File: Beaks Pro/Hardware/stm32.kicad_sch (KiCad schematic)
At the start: 14 parts, among them Q1 2N3904, Q2 2N3904, U8 Bluepill

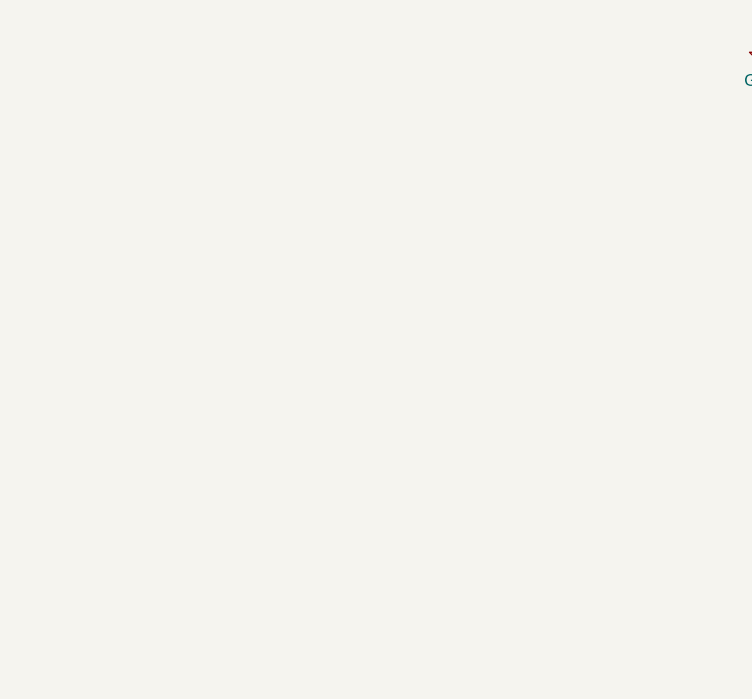
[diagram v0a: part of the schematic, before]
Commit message: Add step files for Bluepill, pots and jacks. Add BOM entries for bluepill headers
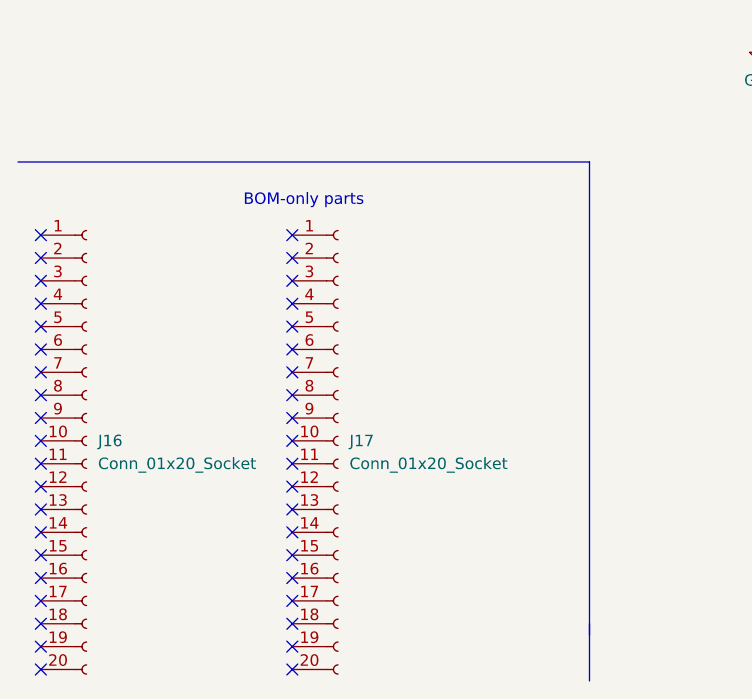
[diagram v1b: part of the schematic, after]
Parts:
- added J16, J17: Conn_01x20_Socket, symbol Connector:Conn_01x20_Socket
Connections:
- no-connect marks 15 -> 55
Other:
- note added: "BOM-only parts"
